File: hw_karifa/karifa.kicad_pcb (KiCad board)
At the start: 2 copper layers, 38.2 x 54.8 mm, 50 parts, among them J1 Conn_2Rows-05Pins, Q1 AO3401A, Q2 AO3401A, Q3 AO3401A, SW1 SW_DPST_x2, T1 Tab, U1 PY32F002AF15P6TU

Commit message: Hópehely routed.
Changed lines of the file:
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@@
   )
   (segment (start 130.186 88.022) (end 129.352 87.188) (width 0.6096) (layer "F.Cu") (net 1))
-  (segment (start 127.05 95.35) (end 129.947 95.35) (width 0.4064) (layer "F.Cu") (net 1))
+  (segment (start 127.05 95.35) (end 129.947 95.35) (width 0.6096) (layer "F.Cu") (net 1))
   (segment (start 123.3807 73.1058) (end 122.24 74.2465) (width 0.4064) (layer "F.Cu") (net 1))
   (segment (start 128.524 85.598) (end 127.762 84.836) (width 0.6096) (layer "F.Cu") (net 1))
@@
   (segment (start 129.352 85.598) (end 128.524 85.598) (width 0.6096) (layer "F.Cu") (net 1))
   (segment (start 129.25 63.0375) (end 128.9375 63.35) (width 0.4064) (layer "F.Cu") (net 1))
-  (segment (start 133.3 95.35) (end 130.425 95.35) (width 0.4064) (layer "F.Cu") (net 1))
+  (segment (start 133.3 95.35) (end 130.425 95.35) (width 0.6096) (layer "F.Cu") (net 1))
   (segment (start 123.19 82.995) (end 122.365 83.82) (width 0.4064) (layer "F.Cu") (net 1))
   (segment (start 129.352 84.648) (end 129.352 85.598) (width 0.4064) (layer "F.Cu") (net 1))

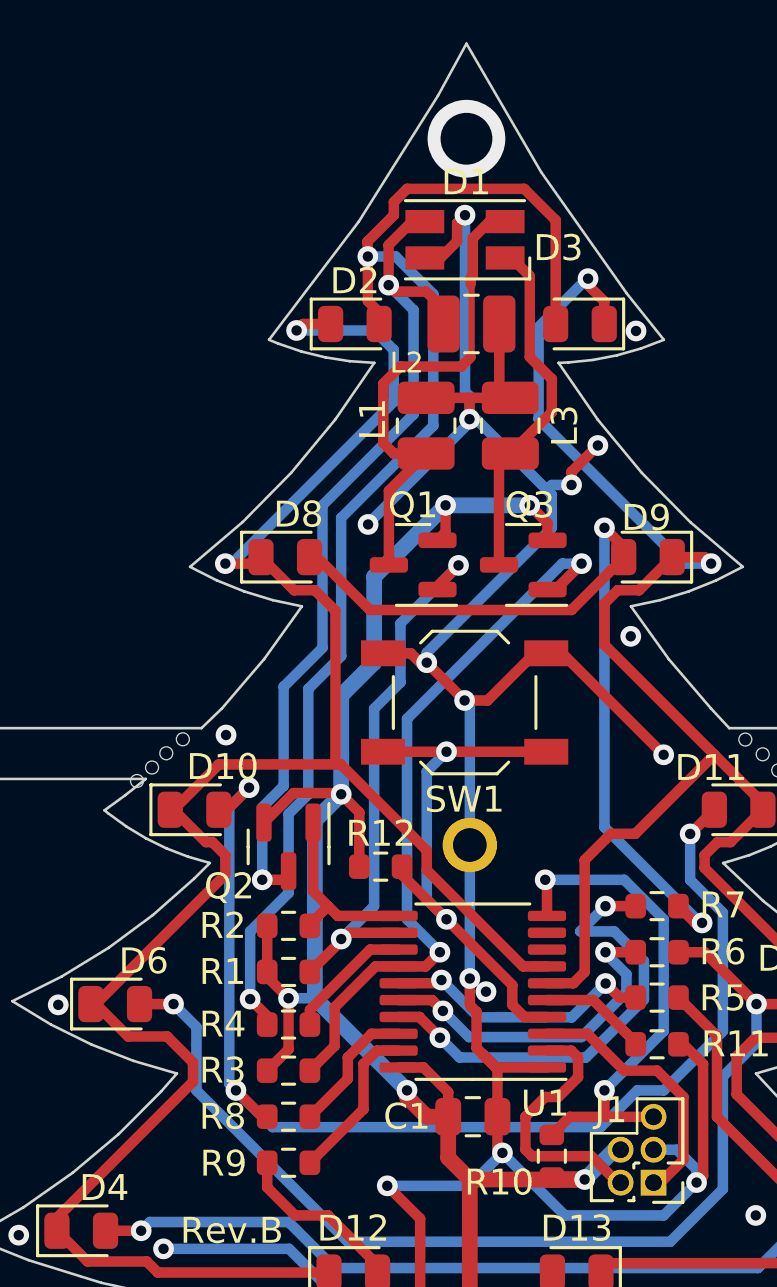
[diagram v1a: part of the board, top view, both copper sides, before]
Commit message: Footprint fix for JLCPCB assembly.
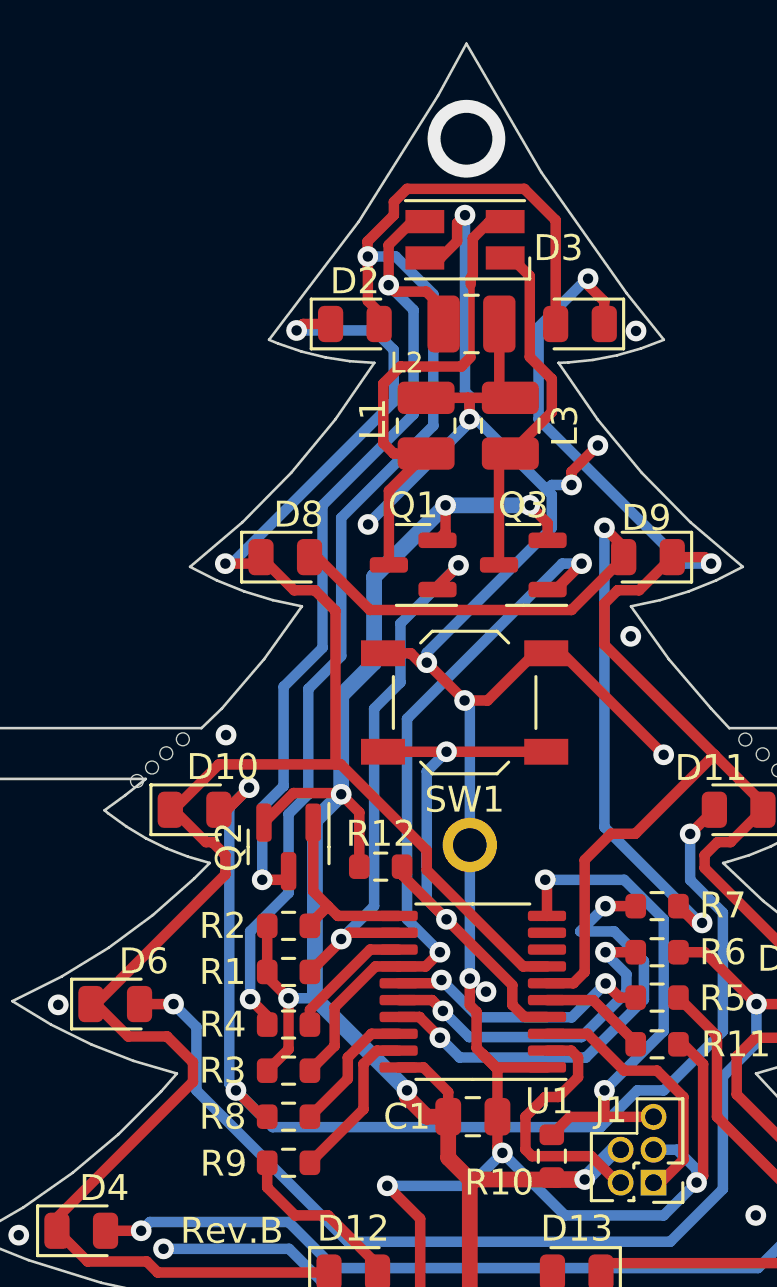
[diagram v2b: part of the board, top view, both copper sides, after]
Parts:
- D1: footprint LED_SMD:LED_RGB_Wuerth-PLCC4_3.2x2.8mm_150141M173100 -> karifa:LED_RGB_Wuerth-PLCC4_3.2x2.8mm_150141M173100
- Q1, Q2, Q3: footprint sajat:SOT-23 -> karifa:SOT-23
- U1: footprint Package_SO:TSSOP-20_4.4x6.5mm_P0.65mm -> karifa:TSSOP-20_4.4x6.5mm_P0.65mm
- turned D1 to 0 degrees
- turned U1 to 0 degrees

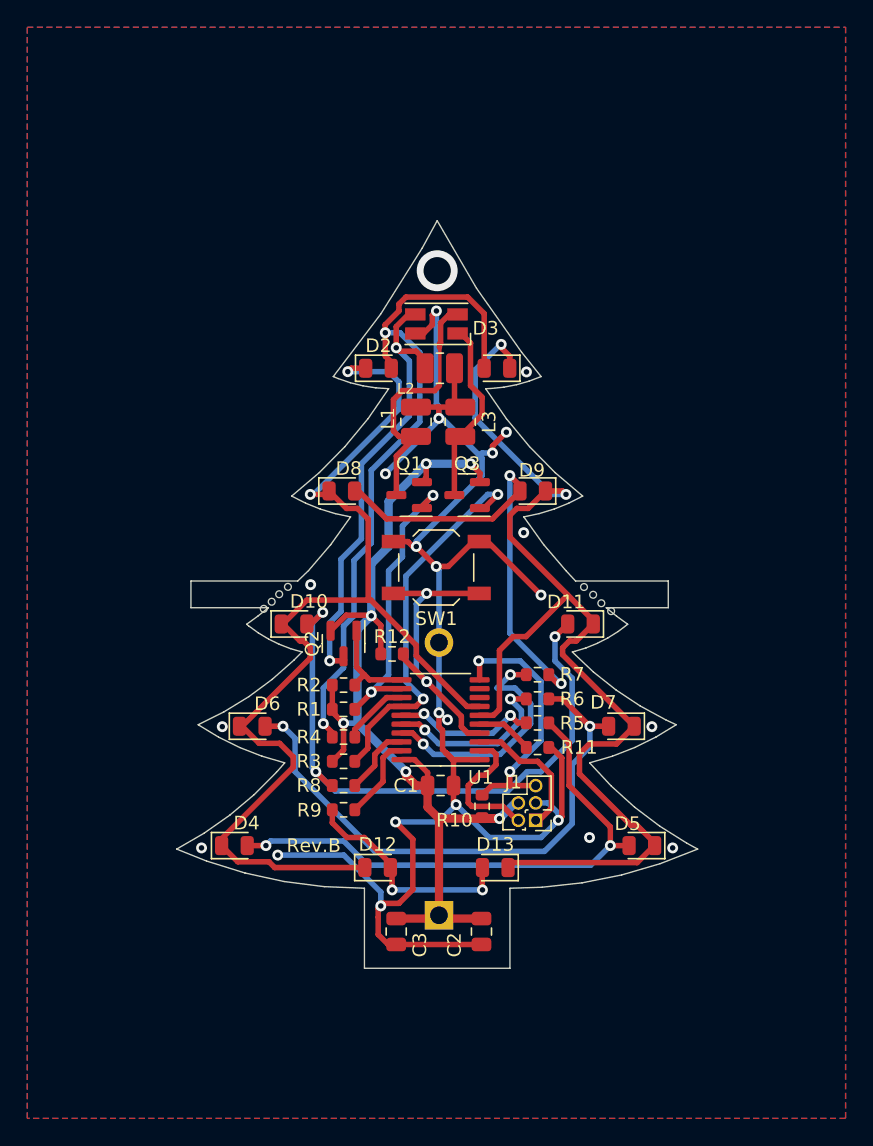
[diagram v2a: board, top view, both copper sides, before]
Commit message: Karifa silkscreen redesigned.
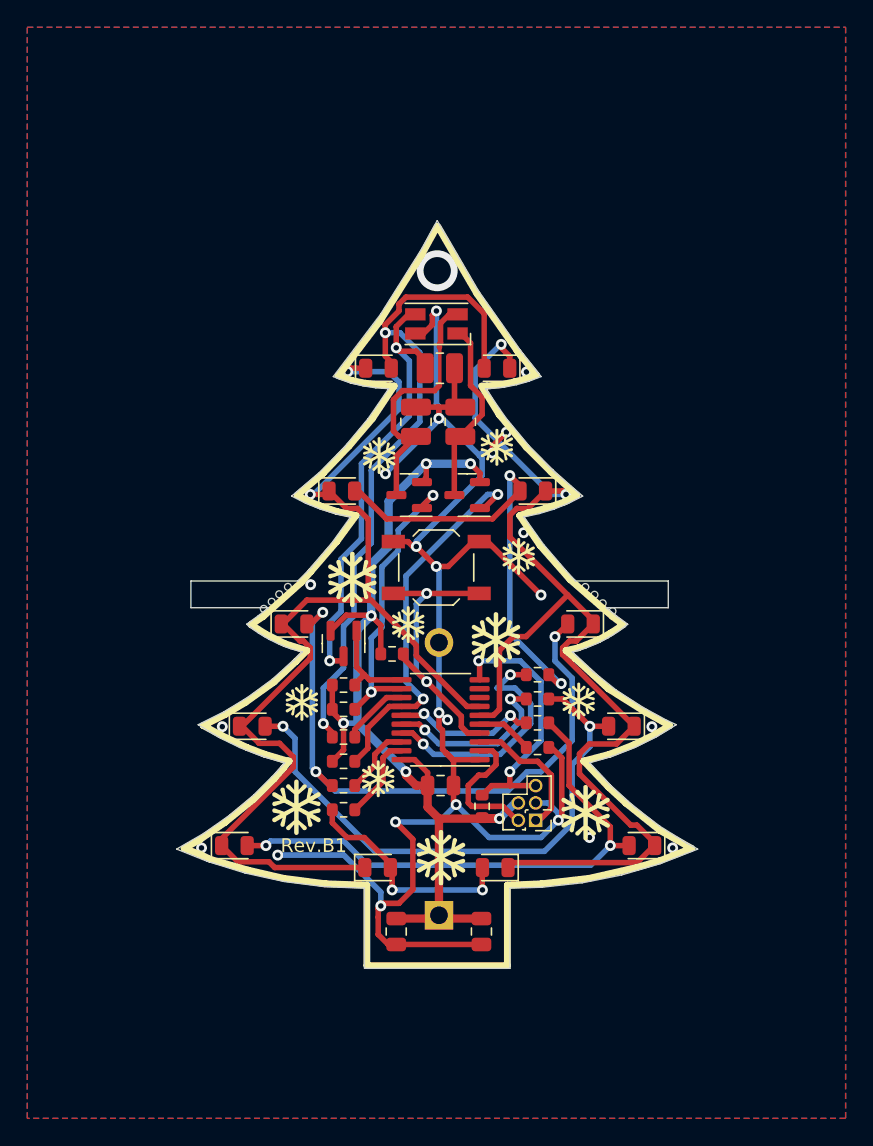
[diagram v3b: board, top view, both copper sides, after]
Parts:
- moved ? 0.10 mm to (142.9, 72.8)
- moved REF** 0.10 mm to (142.2, 72.2)
- moved REF** 0.10 mm to (140.9, 71.0)
- moved REF** 0.10 mm to (141.6, 71.6)
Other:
- board text added: "Rev.B1"
- board text removed: "Rev.B"

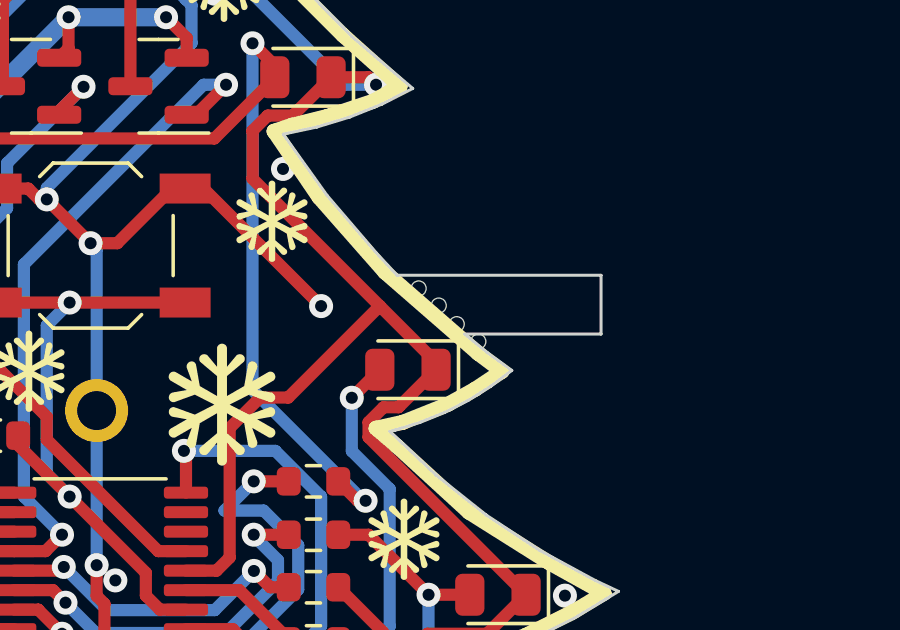
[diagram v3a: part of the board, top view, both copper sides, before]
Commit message: Karifa updated and panelized.
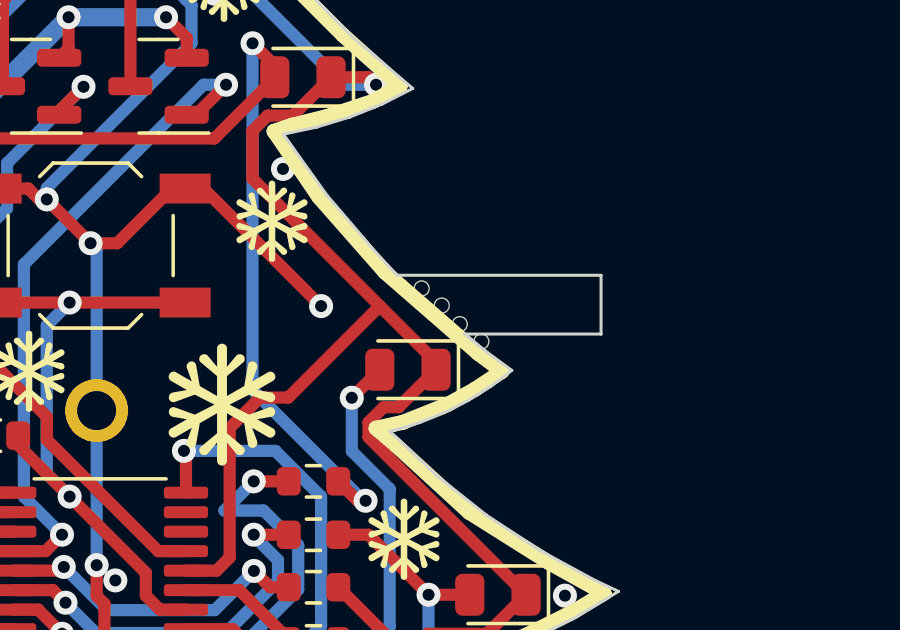
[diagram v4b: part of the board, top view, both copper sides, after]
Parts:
- moved REF** 0.10 mm to (141.0, 71.0)
- moved ? 0.10 mm to (143.0, 72.8)
- moved REF** 0.10 mm to (142.3, 72.2)
- moved REF** 0.10 mm to (141.7, 71.6)
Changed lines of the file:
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@@
 	(footprint "NPTH"
 		(layer "F.Cu")
-		(at 142.19 72.23)
+		(at 142.29 72.23)
 		(property "Reference" "REF**"
 			(at 0 0.5 0)
@@
 			(layer "Dwgs.User")
 		)
-		(fp_text user "KIKIT: width: 10mm"
+		(fp_text user "KIKIT: width: 3mm"
 			(at -5.5 0 0)
 			(layer "Dwgs.User")
@@
 	(footprint "NPTH"
 		(layer "F.Cu")
-		(at 140.92 71.04)
+		(at 141.02 71.04)
 		(property "Reference" "REF**"
 			(at 0 0.5 0)
@@
 	(footprint ""
 		(layer "F.Cu")
-		(at 142.91 72.81)
+		(at 143.01 72.81)
 		(property "Reference" ""
 			(at 0 0 0)
@@
 	(footprint "NPTH"
 		(layer "F.Cu")
-		(at 141.59 71.61)
+		(at 141.69 71.61)
 		(property "Reference" "REF**"
 			(at 0 0.5 0)
